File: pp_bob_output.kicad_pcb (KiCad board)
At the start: 2 copper layers, 98.8 x 72.1 mm, 38 parts, among them P4 13X2, U1 74LS540, U2 74LVC245, U3 74LS541

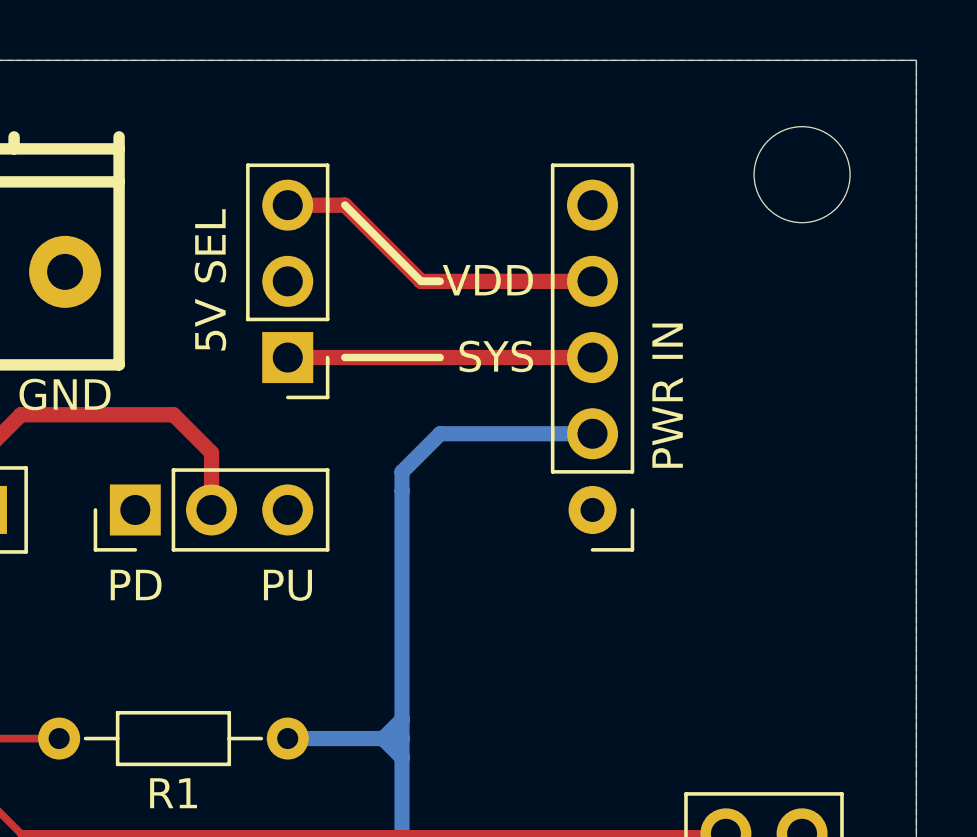
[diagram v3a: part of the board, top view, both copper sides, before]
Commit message: Adjust position of PWR IN & 5V SEL headers
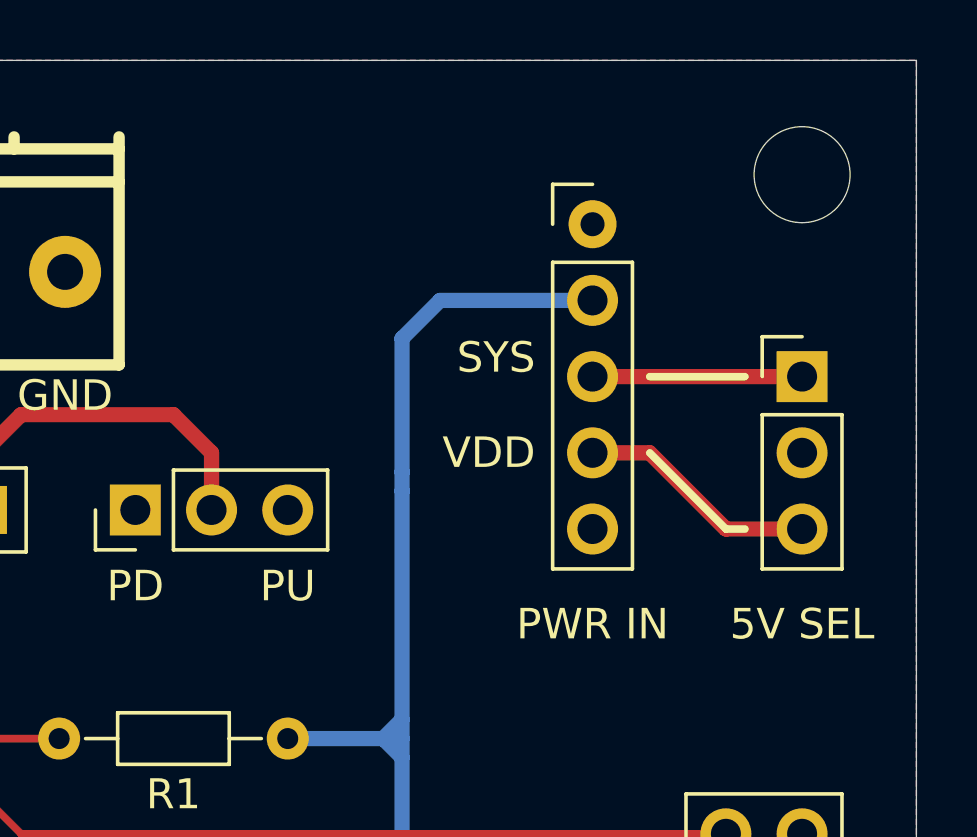
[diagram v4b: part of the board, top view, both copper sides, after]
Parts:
- moved PWRSEL_1 17.2 mm to (120.4, 35.9), turned to 0 degrees
- moved PWRIN_1 9.53 mm to (113.4, 30.9), turned to 0 degrees
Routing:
- net +3V3: track 167.4 -> 171.8 mm
- net /VDD_+5v: track 11.2 -> 8.04 mm
- net /SYS_+5v: track 10.2 -> 6.98 mm
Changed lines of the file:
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@@
-(kicad_pcb (version 4) (host pcbnew 4.0.6-e0-6349~53~ubuntu16.04.1)
+(kicad_pcb (version 20170123) (host pcbnew no-vcs-found-ecdfa40~58~ubuntu16.04.1)
   (general
     (links 129)
     (no_connects 0)
-    (area 25.387299 25.387299 124.218701 97.548701)
+    (area 25.095 24.0525 124.432905 99.0185)
     (thickness 1.6)
     (drawings 75)
-    (tracks 357)
+    (tracks 358)
     (zones 0)
     (modules 38)
@@
   )
   (setup
-    (last_trace_width 0.381)
+    (last_trace_width 0.508)
     (user_trace_width 0.0254)
     (user_trace_width 0.254)
@@
       (hpglpenspeed 20)
       (hpglpendiameter 15)
-      (hpglpenoverlay 2)
       (psnegative false)
       (psa4output false)
@@
   )
   (module Pin_Headers:Pin_Header_Straight_1x05_Pitch2.54mm (layer F.Cu)
-    (at 113.411 40.386 180)
+    (at 113.411 30.861)
     (descr "Through hole straight pin header, 1x05, 2.54mm pitch, single row")
     (tags "Through hole pin header THT 1x05 2.54mm single row")
-    (fp_text reference PWRIN_1 (at 0 -2.33 180) (layer F.SilkS) hide
-      (effects (font (size 1 1) (thickness 0.15)))
-    )
-    (fp_text value 1X5 (at 0 12.49 180) (layer F.Fab) hide
-      (effects (font (size 1 1) (thickness 0.15)))
-    )
-    (fp_text user %R (at 0 -2.33 270) (layer F.Fab)
+    (fp_text reference PWRIN_1 (at 0 -2.33) (layer F.SilkS) hide
+      (effects (font (size 1 1) (thickness 0.15)))
+    )
+    (fp_text value 1X5 (at 0 12.49) (layer F.Fab) hide
+      (effects (font (size 1 1) (thickness 0.15)))
+    )
+    (fp_text user %R (at 0 -2.33 90) (layer F.Fab)
       (effects (font (size 1 1) (thickness 0.15)))
     )
@@
     (fp_line (start -1.27 11.43) (end 1.27 11.43) (layer F.Fab) (width 0.1))
     (fp_line (start -1.27 -1.27) (end -1.27 11.43) (layer F.Fab) (width 0.1))
-    (pad 5 thru_hole oval (at 0 10.16 180) (size 1.7 1.7) (drill 1) (layers *.Cu *.Mask))
-    (pad 4 thru_hole oval (at 0 7.62 180) (size 1.7 1.7) (drill 1) (layers *.Cu *.Mask)
+    (pad 5 thru_hole oval (at 0 10.16) (size 1.7 1.7) (drill 1) (layers *.Cu *.Mask))
+    (pad 4 thru_hole oval (at 0 7.62) (size 1.7 1.7) (drill 1) (layers *.Cu *.Mask)
       (net 31 /VDD_+5v))
-    (pad 3 thru_hole oval (at 0 5.08 180) (size 1.7 1.7) (drill 1) (layers *.Cu *.Mask)
+    (pad 3 thru_hole oval (at 0 5.08) (size 1.7 1.7) (drill 1) (layers *.Cu *.Mask)
       (net 30 /SYS_+5v))
-    (pad 2 thru_hole oval (at 0 2.54 180) (size 1.7 1.7) (drill 1) (layers *.Cu *.Mask)
+    (pad 2 thru_hole oval (at 0 2.54) (size 1.7 1.7) (drill 1) (layers *.Cu *.Mask)
       (net 2 +3V3))
-    (pad 1 thru_hole circle (at 0 0 180) (size 1.6 1.6) (drill 0.8) (layers *.Cu *.Mask)
+    (pad 1 thru_hole circle (at 0 0) (size 1.6 1.6) (drill 0.8) (layers *.Cu *.Mask)
       (net 1 GND))
     (model ${KISYS3DMOD}/Pin_Headers.3dshapes/Pin_Header_Straight_1x05_Pitch2.54mm.wrl
@@
   )
   (module Pin_Headers:Pin_Header_Straight_1x03_Pitch2.54mm (layer F.Cu)
-    (at 103.251 35.306 180)
+    (at 120.396 35.941)
     (descr "Through hole straight pin header, 1x03, 2.54mm pitch, single row")
     (tags "Through hole pin header THT 1x03 2.54mm single row")
-    (fp_text reference PWRSEL_1 (at 0 -2.33 180) (layer F.SilkS) hide
-      (effects (font (size 1 1) (thickness 0.15)))
-    )
-    (fp_text value 1X3 (at 0 7.41 180) (layer F.Fab) hide
-      (effects (font (size 1 1) (thickness 0.15)))
-    )
-    (fp_text user %R (at 0 -2.33 180) (layer F.Fab)
+    (fp_text reference PWRSEL_1 (at 0 -2.33) (layer F.SilkS) hide
+      (effects (font (size 1 1) (thickness 0.15)))
+    )
+    (fp_text value 1X3 (at 0 7.41) (layer F.Fab) hide
+      (effects (font (size 1 1) (thickness 0.15)))
+    )
+    (fp_text user %R (at 0 -2.33) (layer F.Fab)
       (effects (font (size 1 1) (thickness 0.15)))
     )
@@
     (fp_line (start -1.27 6.35) (end 1.27 6.35) (layer F.Fab) (width 0.1))
     (fp_line (start -1.27 -1.27) (end -1.27 6.35) (layer F.Fab) (width 0.1))
-    (pad 3 thru_hole oval (at 0 5.08 180) (size 1.7 1.7) (drill 1) (layers *.Cu *.Mask)
+    (pad 3 thru_hole oval (at 0 5.08) (size 1.7 1.7) (drill 1) (layers *.Cu *.Mask)
       (net 31 /VDD_+5v))
-    (pad 2 thru_hole oval (at 0 2.54 180) (size 1.7 1.7) (drill 1) (layers *.Cu *.Mask)
+    (pad 2 thru_hole oval (at 0 2.54) (size 1.7 1.7) (drill 1) (layers *.Cu *.Mask)
       (net 3 +5V))
-    (pad 1 thru_hole rect (at 0 0 180) (size 1.7 1.7) (drill 1) (layers *.Cu *.Mask)
+    (pad 1 thru_hole rect (at 0 0) (size 1.7 1.7) (drill 1) (layers *.Cu *.Mask)
       (net 30 /SYS_+5v))
     (model ${KISYS3DMOD}/Pin_Headers.3dshapes/Pin_Header_Straight_1x03_Pitch2.54mm.wrl
@@
     (descr "20-lead dip package, row spacing 7.62 mm (300 mils), LongPads")
     (tags "DIL DIP PDIP 2.54mm 7.62mm 300mil LongPads")
-    (fp_text reference U1 (at 3.81 -2.39 450) (layer F.SilkS)
+    (fp_text reference U1 (at 3.81 -2.39 90) (layer F.SilkS)
       (effects (font (size 1 1) (thickness 0.15)))
     )
@@
     )
   )
-  (gr_line (start 107.696 32.766) (end 105.156 30.226) (angle 90) (layer F.SilkS) (width 0.254))
-  (gr_line (start 108.331 32.766) (end 107.696 32.766) (angle 90) (layer F.SilkS) (width 0.254))
-  (gr_line (start 108.331 35.306) (end 105.156 35.306) (angle 90) (layer F.SilkS) (width 0.254))
+  (gr_line (start 117.856 41.021) (end 115.316 38.481) (angle 90) (layer F.SilkS) (width 0.254))
+  (gr_line (start 118.491 41.021) (end 117.856 41.021) (angle 90) (layer F.SilkS) (width 0.254))
+  (gr_line (start 118.491 35.941) (end 115.316 35.941) (angle 90) (layer F.SilkS) (width 0.254))
   (gr_line (start 44.196 37.846) (end 44.196 36.576) (angle 90) (layer F.SilkS) (width 0.254))
-  (gr_text "5V SEL" (at 100.711 32.766 90) (layer F.SilkS)
+  (gr_text "5V SEL" (at 120.396 44.196) (layer F.SilkS)
     (effects (font (size 1.016 1.016) (thickness 0.2032)))
   )
@@
     (effects (font (size 1.016 1.016) (thickness 0.2032)))
   )
-  (gr_text "PWR IN" (at 115.951 36.576 90) (layer F.SilkS)
-    (effects (font (size 1.016 1.016) (thickness 0.2032)))
-  )
-  (gr_text VDD (at 111.506 32.766) (layer F.SilkS)
+  (gr_text "PWR IN" (at 113.411 44.196) (layer F.SilkS)
+    (effects (font (size 1.016 1.016) (thickness 0.2032)))
+  )
+  (gr_text VDD (at 111.506 38.481) (layer F.SilkS)
     (effects (font (size 1.016 1.016) (thickness 0.2032)) (justify right))
   )
@@
   (segment (start 100.711 71.501) (end 100.711 72.851) (width 0.508) (layer F.Cu) (net 1))
   (segment (start 99.441 70.231) (end 100.711 71.501) (width 0.508) (layer F.Cu) (net 1))
+  (segment (start 107.061 39.116) (end 107.061 34.671) (width 0.508) (layer B.Cu) (net 2))
+  (segment (start 108.331 33.401) (end 113.411 33.401) (width 0.508) (layer B.Cu) (net 2))
+  (segment (start 107.061 34.671) (end 108.331 33.401) (width 0.508) (layer B.Cu) (net 2))
   (segment (start 47.371 42.291) (end 45.466 42.291) (width 0.381) (layer B.Cu) (net 2))
   (segment (start 49.911 52.451) (end 49.911 80.391) (width 0.508) (layer B.Cu) (net 2))
@@
   (segment (start 46.101 80.391) (end 49.276 80.391) (width 0.508) (layer B.Cu) (net 2))
   (segment (start 107.061 39.751) (end 107.061 39.116) (width 0.508) (layer B.Cu) (net 2))
-  (segment (start 108.331 37.846) (end 113.411 37.846) (width 0.508) (layer B.Cu) (net 2))
-  (segment (start 107.061 39.116) (end 108.331 37.846) (width 0.508) (layer B.Cu) (net 2))
   (segment (start 107.061 47.371) (end 106.426 48.006) (width 0.508) (layer B.Cu) (net 2))
   (segment (start 107.061 48.641) (end 106.426 48.006) (width 0.508) (layer B.Cu) (net 2))
@@
   (segment (start 82.296 58.801) (end 111.506 58.801) (width 0.254) (layer F.Cu) (net 29))
   (segment (start 80.391 56.896) (end 82.296 58.801) (width 0.254) (layer F.Cu) (net 29))
-  (segment (start 103.251 35.306) (end 113.411 35.306) (width 0.508) (layer F.Cu) (net 30))
-  (segment (start 103.251 30.226) (end 105.156 30.226) (width 0.508) (layer F.Cu) (net 31))
-  (segment (start 107.696 32.766) (end 113.411 32.766) (width 0.508) (layer F.Cu) (net 31))
-  (segment (start 105.156 30.226) (end 107.696 32.766) (width 0.508) (layer F.Cu) (net 31))
+  (segment (start 113.411 35.941) (end 120.396 35.941) (width 0.508) (layer F.Cu) (net 30) (status C00000))
+  (segment (start 113.411 38.481) (end 115.316 38.481) (width 0.508) (layer F.Cu) (net 31) (status 400000))
+  (segment (start 117.856 41.021) (end 120.396 41.021) (width 0.508) (layer F.Cu) (net 31) (status 800000))
+  (segment (start 115.316 38.481) (end 117.856 41.021) (width 0.508) (layer F.Cu) (net 31))
   (segment (start 93.091 48.3235) (end 93.4085 48.006) (width 0.254) (layer F.Cu) (net 32))
   (segment (start 93.091 48.3235) (end 92.7735 48.006) (width 0.254) (layer F.Cu) (net 32))
